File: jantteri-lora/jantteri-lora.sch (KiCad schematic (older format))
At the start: 0 parts

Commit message: Lora PCB desging
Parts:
- added FB1: GZ2012D101TF, Inductor_SMD:L_0805_2012Metric, symbol Device:Ferrite_Bead
- added U1: lora-mod, RF_Module:HOPERF_RFM69HW, symbol voja-lib:lora-mod
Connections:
- net AMS1117-3.3/VIN: now also FB1.1
- net GND: now also U1.12 (GND)
- new net 5V-IN: U1.11 (VCC)
- new net DATA1: U1.3 (D1)
- new net DATA10: U1.14 (D10)
- new net DATA11: U1.15 (D11)
- new net DATA12: U1.16 (D12)
- new net DATA13: U1.17 (D13)
- new net DATA14: U1.18 (D14)
- new net DATA15: U1.19 (D15)
- new net DATA16: U1.20 (D16)
- new net DATA2: U1.4 (D2)
- new net DATA3: U1.5 (D3)
- new net DATA4: U1.6 (D4)
- new net DATA5: U1.7 (D5)
- new net DATA6: U1.8 (D6)
- new net DATA7: U1.9 (D7)
- new net DATA8: U1.10 (D8)
- new net DATA9: U1.13 (D9)
- new net OUTPUT_SCL: U1.2 (LORA_SCL)
- new net OUTPUT_SDA: U1.1 (LORA_SDA)
- new net power_protect/OUT: FB1.2
- no-connect marks 1 -> 2
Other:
- note added: "5V-IN disables USB power input. If no 5V-IN connected, USB-5V is used"

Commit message: Lora-module v1
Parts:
- U1: footprint RF_Module:HOPERF_RFM69HW -> voja-footprints:lora-mod; symbol voja-lib:lora-mod -> jantteri-lora-rescue:lora-mod-voja-lib
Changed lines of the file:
@@
 $EndSheet
 $Comp
-L power:+3V3 #PWR0101
+L power:+3V3 #PWR08
 U 1 1 61143103
 P 5850 1850
-F 0 "#PWR0101" H 5850 1700 50  0001 C CNN
+F 0 "#PWR08" H 5850 1700 50  0001 C CNN
 F 1 "+3V3" H 5865 2023 50  0000 C CNN
 F 2 "" H 5850 1850 50  0001 C CNN
@@
 $EndComp
 $Comp
-L power:GND #PWR0102
+L power:GND #PWR09
 U 1 1 611435CD
 P 5850 1950
-F 0 "#PWR0102" H 5850 1700 50  0001 C CNN
+F 0 "#PWR09" H 5850 1700 50  0001 C CNN
 F 1 "GND" H 5855 1777 50  0000 C CNN
 F 2 "" H 5850 1950 50  0001 C CNN
@@
 	6100 2600 5900 2600
 $Comp
-L power:GND #PWR0103
+L power:GND #PWR07
 U 1 1 611483EC
 P 5050 2500
-F 0 "#PWR0103" H 5050 2250 50  0001 C CNN
+F 0 "#PWR07" H 5050 2250 50  0001 C CNN
 F 1 "GND" H 5055 2327 50  0000 C CNN
 F 2 "" H 5050 2500 50  0001 C CNN
@@
 $EndComp
 $Comp
-L power:GND #PWR0104
+L power:GND #PWR010
 U 1 1 61148B21
 P 7950 2900
-F 0 "#PWR0104" H 7950 2650 50  0001 C CNN
+F 0 "#PWR010" H 7950 2650 50  0001 C CNN
 F 1 "GND" H 7955 2727 50  0000 C CNN
 F 2 "" H 7950 2900 50  0001 C CNN
@@
 $EndComp
 $Comp
-L power:+3V3 #PWR0105
+L power:+3V3 #PWR06
 U 1 1 61148EAA
 P 5050 2400
-F 0 "#PWR0105" H 5050 2250 50  0001 C CNN
+F 0 "#PWR06" H 5050 2250 50  0001 C CNN
 F 1 "+3V3" H 5065 2573 50  0000 C CNN
 F 2 "" H 5050 2400 50  0001 C CNN
@@
 	5250 2400 5050 2400
 $Comp
-L power:+3V3 #PWR0106
+L power:+3V3 #PWR011
 U 1 1 6114B431
 P 8900 1350
-F 0 "#PWR0106" H 8900 1200 50  0001 C CNN
+F 0 "#PWR011" H 8900 1200 50  0001 C CNN
 F 1 "+3V3" H 8915 1523 50  0000 C CNN
 F 2 "" H 8900 1350 50  0001 C CNN
@@
 $EndComp
 $Comp
-L power:GND #PWR0107
+L power:GND #PWR012
 U 1 1 6114B78E
 P 8900 1450
-F 0 "#PWR0107" H 8900 1200 50  0001 C CNN
+F 0 "#PWR012" H 8900 1200 50  0001 C CNN
 F 1 "GND" H 8905 1277 50  0000 C CNN
 F 2 "" H 8900 1450 50  0001 C CNN
@@
 	8700 1350 8900 1350
 $Comp
-L power:GND #PWR0108
+L power:GND #PWR03
 U 1 1 6114C811
 P 3550 1650
-F 0 "#PWR0108" H 3550 1400 50  0001 C CNN
+F 0 "#PWR03" H 3550 1400 50  0001 C CNN
 F 1 "GND" H 3555 1477 50  0000 C CNN
 F 2 "" H 3550 1650 50  0001 C CNN
@@
 	3550 1650 3650 1650
 $Comp
-L power:+3V3 #PWR0110
+L power:+3V3 #PWR05
 U 1 1 6114D52E
 P 4550 1550
-F 0 "#PWR0110" H 4550 1400 50  0001 C CNN
+F 0 "#PWR05" H 4550 1400 50  0001 C CNN
 F 1 "+3V3" H 4565 1723 50  0000 C CNN
 F 2 "" H 4550 1550 50  0001 C CNN
@@
 5V-IN
 $Comp
-L power:GND #PWR0109
+L power:GND #PWR04
 U 1 1 61169965
 P 3650 3550
-F 0 "#PWR0109" H 3650 3300 50  0001 C CNN
+F 0 "#PWR04" H 3650 3300 50  0001 C CNN
 F 1 "GND" H 3655 3377 50  0000 C CNN
 F 2 "" H 3650 3550 50  0001 C CNN
@@
 DATA1
 $Comp
-L voja-lib:lora-mod U1
+L jantteri-lora-rescue:lora-mod-voja-lib U1
 U 1 1 61170943
 P 2700 3800
 F 0 "U1" H 2675 4375 50  0000 C CNN
 F 1 "lora-mod" H 2675 4284 50  0000 C CNN
-F 2 "RF_Module:HOPERF_RFM69HW" H 2700 3800 50  0001 C CNN
+F 2 "voja-footprints:lora-mod" H 2700 3800 50  0001 C CNN
 F 3 "" H 2700 3800 50  0001 C CNN
 	1    2700 3800
@@
 Connection ~ 2350 1550
 $Comp
-L power:GND #PWR0111
+L power:GND #PWR01
 U 1 1 611AB45E
 P 2100 1600
-F 0 "#PWR0111" H 2100 1350 50  0001 C CNN
+F 0 "#PWR01" H 2100 1350 50  0001 C CNN
 F 1 "GND" H 2105 1427 50  0000 C CNN
 F 2 "" H 2100 1600 50  0001 C CNN
@@
 $EndComp
 $Comp
-L power:GND #PWR0112
+L power:GND #PWR02
 U 1 1 611AB5EF
 P 2100 2300
-F 0 "#PWR0112" H 2100 2050 50  0001 C CNN
+F 0 "#PWR02" H 2100 2050 50  0001 C CNN
 F 1 "GND" H 2105 2127 50  0000 C CNN
 F 2 "" H 2100 2300 50  0001 C CNN

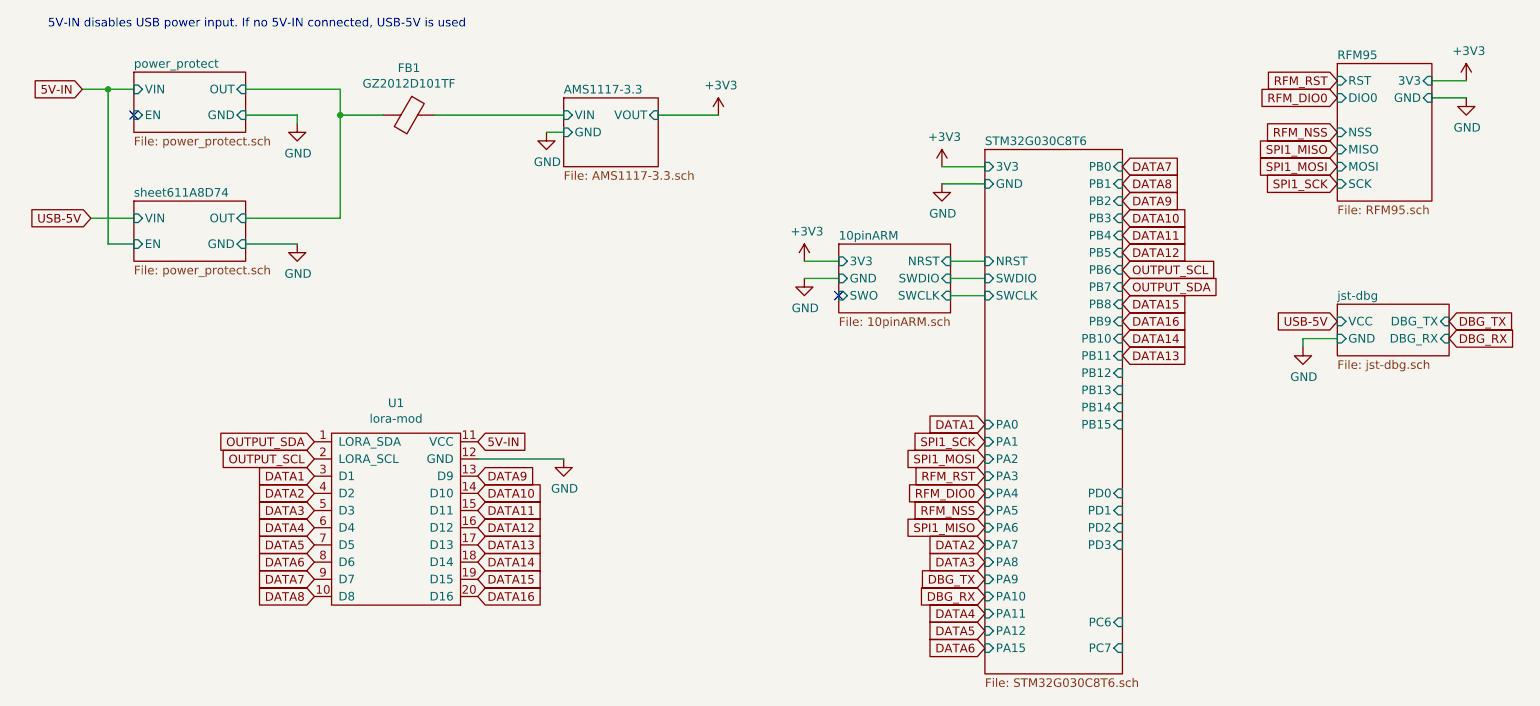
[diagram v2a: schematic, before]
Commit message: Tuubijantteri design Ordered
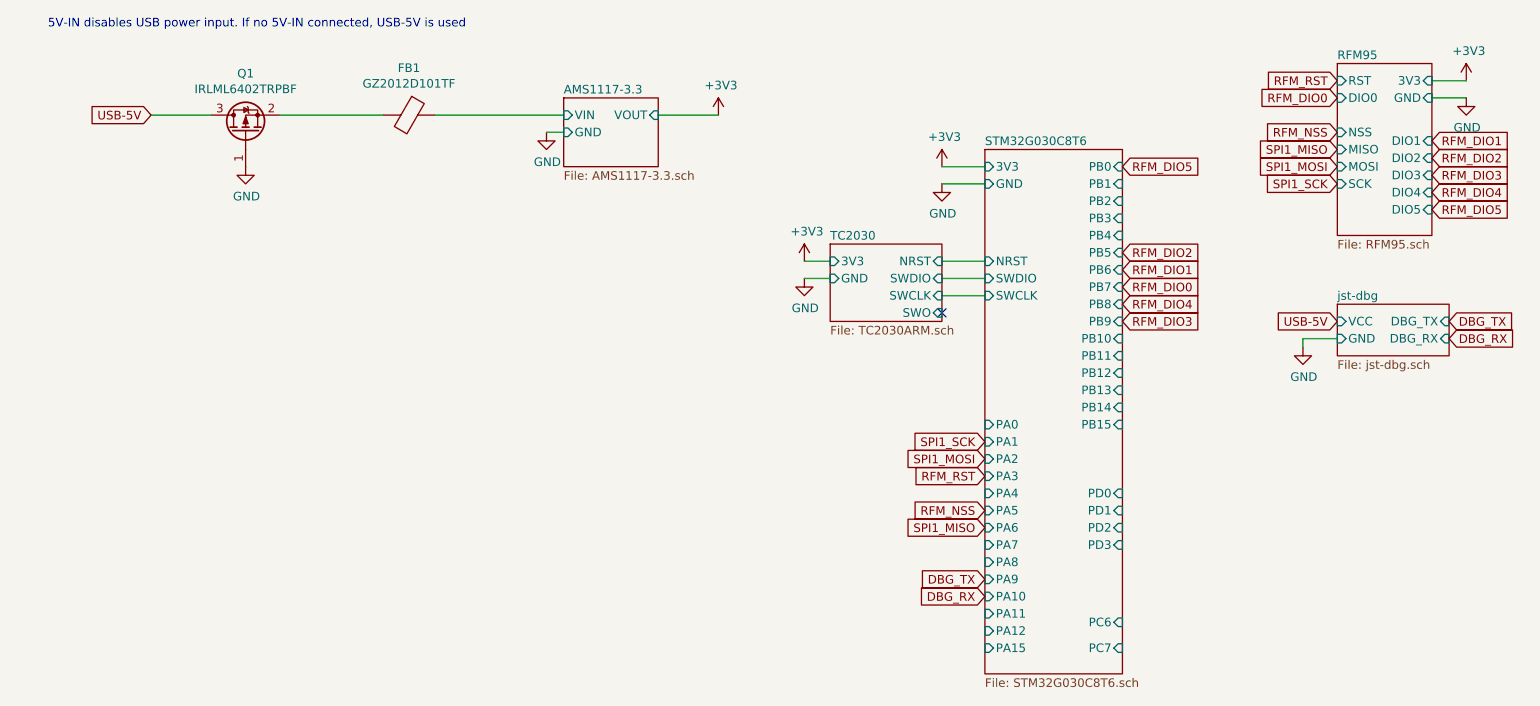
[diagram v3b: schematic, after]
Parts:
- removed U1: lora-mod, voja-footprints:lora-mod, symbol jantteri-lora-rescue:lora-mod-voja-lib
- added Q1: IRLML6402TRPBF, Package_TO_SOT_SMD:SOT-23, symbol Transistor_FET:Si2319CDS
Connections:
- net GND: now also Q1.1 (G)
- net USB-5V: now also Q1.3 (D)
- net power_protect/OUT: no longer names the net of FB1.2
- net power_protect/OUT: now also Q1.2 (S)
- no-connect marks 2 -> 1
